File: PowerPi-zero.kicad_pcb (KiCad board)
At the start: 2 copper layers, 65 x 30 mm, 54 parts, among them IC2 TPS51397ARJER, J1 2444, J2 JST XH 01x02, J6 Raspberry_Pi_2_3, J8 JST XH 01x02, Q1 SiA471DJ, Q2 SiA430DJT, U1 LM74700

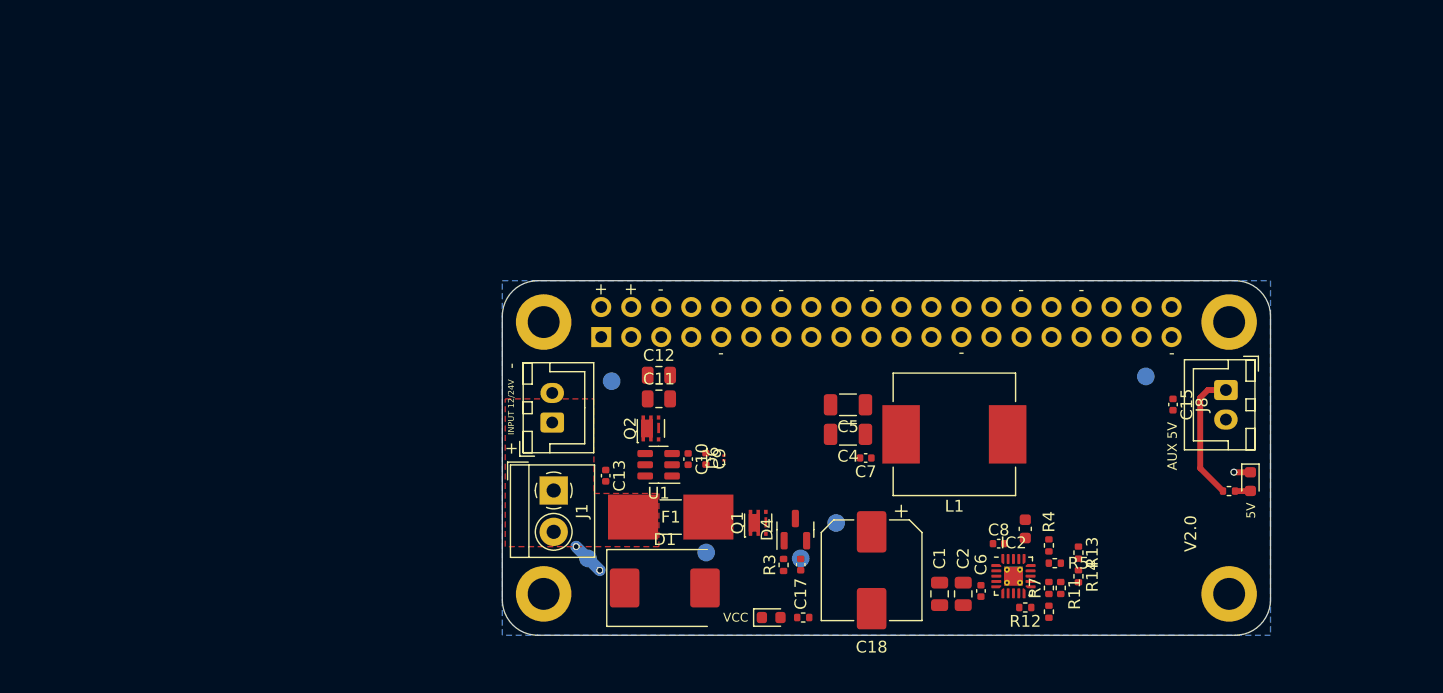
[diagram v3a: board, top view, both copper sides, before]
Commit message: update component position, better layout
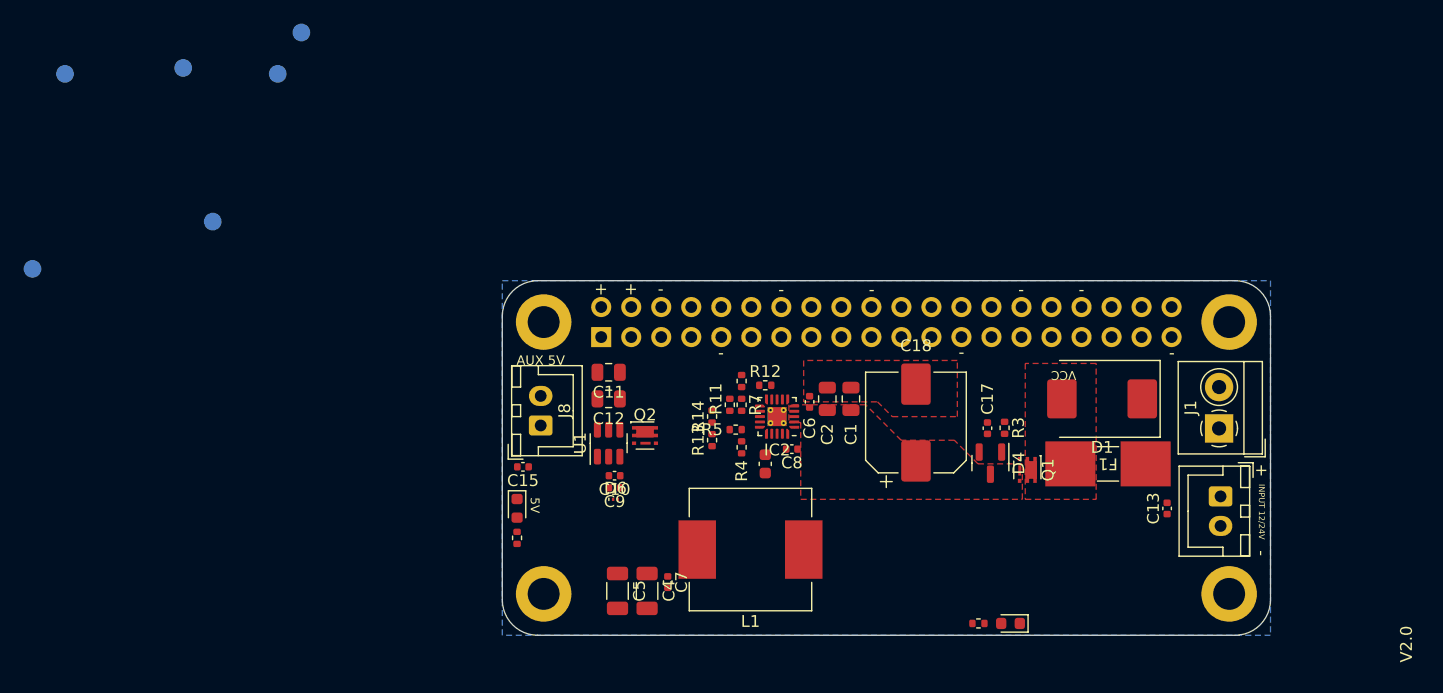
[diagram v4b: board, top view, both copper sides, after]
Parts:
- moved TP1 80.0 mm to (65.2, 88.5)
- moved D3 62.1 mm to (91.0, 112.8)
- moved TP4 61.4 mm to (72.8, 72.5)
- moved R6 60.4 mm to (91.0, 115.3), turned to -90 degrees
- moved TP2 60.3 mm to (52.8, 76.0)
- moved TP3 60.3 mm to (62.8, 75.5)
- moved TP6 60.3 mm to (70.8, 76.0)
- moved J8 58.1 mm to (93.0, 105.8), turned to 90 degrees
- moved J2 56.9 mm to (150.5, 111.8), turned to -90 degrees
- moved J1 56.5 mm to (150.4, 106.0), turned to 90 degrees
- moved C15 55.3 mm to (91.5, 109.2), turned to 180 degrees
- moved TP5 49.9 mm to (50.0, 92.5)
- moved C13 47.6 mm to (146.0, 112.8), turned to 90 degrees
- moved D1 40.3 mm to (140.5, 103.5), turned to 180 degrees
- moved F1 37.3 mm to (141.0, 109.0), turned to 180 degrees
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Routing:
- net +5V: track 11.1 -> 0.00 mm
- net Net-(J1-Pin_1): track 2.83 -> 0.00 mm, vias 2 -> 0
- net GND: track 1.41 -> 0.00 mm, vias 1 -> 0
- net Net-(D3-A): track 1.29 -> 0.00 mm
- added copper zone on F.Cu, net GND
- added copper zone on F.Cu, net Net-(D1-A2)
- added copper zone on F.Cu, net Vin
- removed copper zone on F.Cu, net Net-(J1-Pin_1)

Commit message: layout drafted, silk issues remain
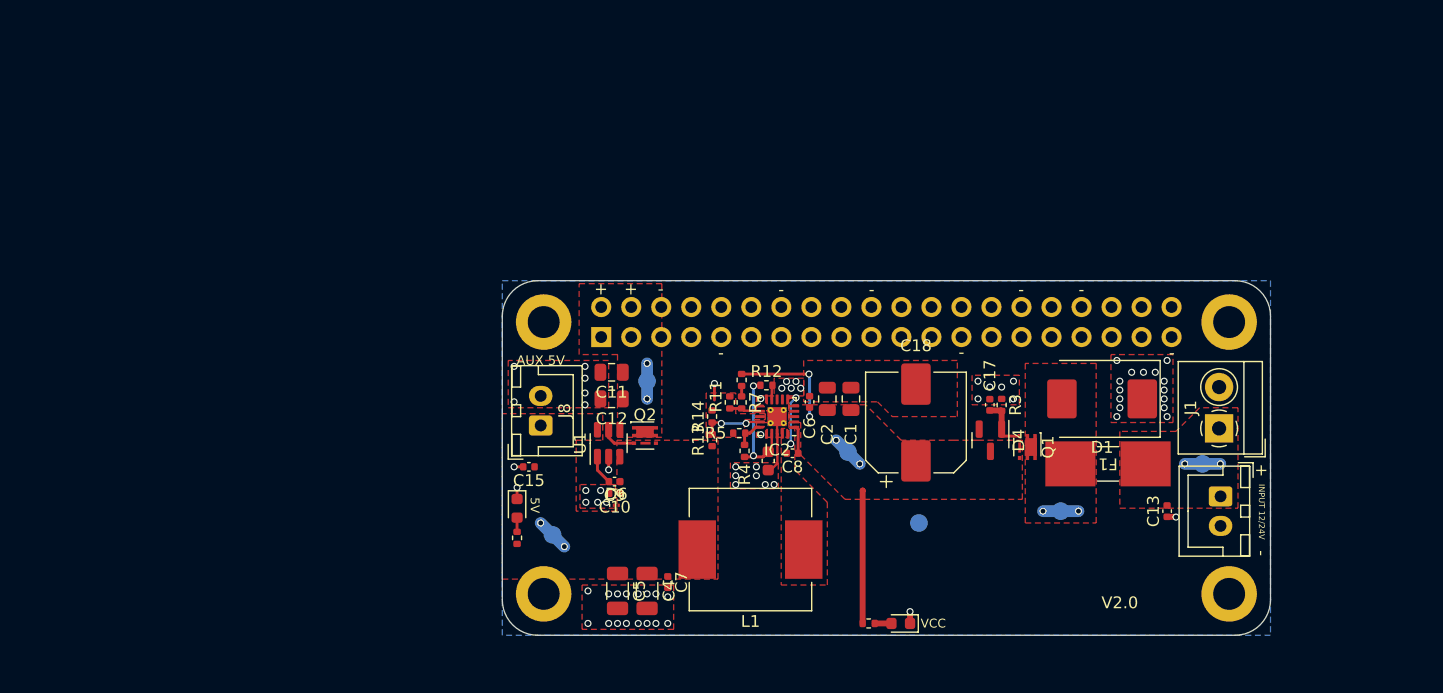
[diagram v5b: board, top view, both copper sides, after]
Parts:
- moved TP2 101.8 mm to (149.0, 109.0)
- moved TP3 83.2 mm to (137.0, 113.0)
- moved TP6 66.2 mm to (125.0, 114.0)
- moved TP4 58.3 mm to (119.0, 108.0)
- moved TP5 52.9 mm to (102.0, 102.0)
- moved TP1 39.1 mm to (94.0, 115.0)
- moved G*** 22.6 mm to (118.0, 117.0)
- moved D5 9.29 mm to (123.5, 122.5)
- moved R8 9.29 mm to (120.8, 122.5)
- moved G*** 9.08 mm to (140.5, 118.0)
- moved C17 1.99 mm to (131.0, 104.0)
- moved R3 1.95 mm to (132.0, 104.0)
- moved D4 1.94 mm to (131.1, 107.0)
- moved Q1 1.94 mm to (134.2, 107.6)
- moved C10 1.50 mm to (99.3, 111.5)
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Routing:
- net Vin: track 0.00 -> 23.4 mm, vias 0 -> 4
- net GND: track 0.00 -> 11.0 mm, vias 0 -> 68
- net VCC: track 0.00 -> 10.4 mm, vias 0 -> 2
- net FB: track 0.00 -> 5.12 mm, vias 0 -> 2
- net SW: track 0.00 -> 4.85 mm, vias 0 -> 2
- net Net-(D4-A): track 0.00 -> 4.67 mm
- net Net-(Q2-G): track 0.00 -> 3.01 mm
- net Net-(J1-Pin_1): track 0.00 -> 3.00 mm, vias 0 -> 2
- net Net-(D1-A2): track 0.00 -> 3.00 mm, vias 0 -> 2
- net 5V_PI: track 0.00 -> 3.00 mm, vias 0 -> 2
- net +5V: track 0.00 -> 2.83 mm, vias 0 -> 2
- net Net-(IC2-EN): track 0.00 -> 2.65 mm
- net Net-(U1-VCAP): track 0.00 -> 2.51 mm
- net Net-(IC2-MODE): track 0.00 -> 2.46 mm
- net BST: track 0.00 -> 2.44 mm
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- added copper zone on F.Cu, net +5V
- added copper zone on F.Cu, net 5V_PI
- added copper zone on F.Cu, net Net-(J1-Pin_1)
- added copper zone on F.Cu, net SW

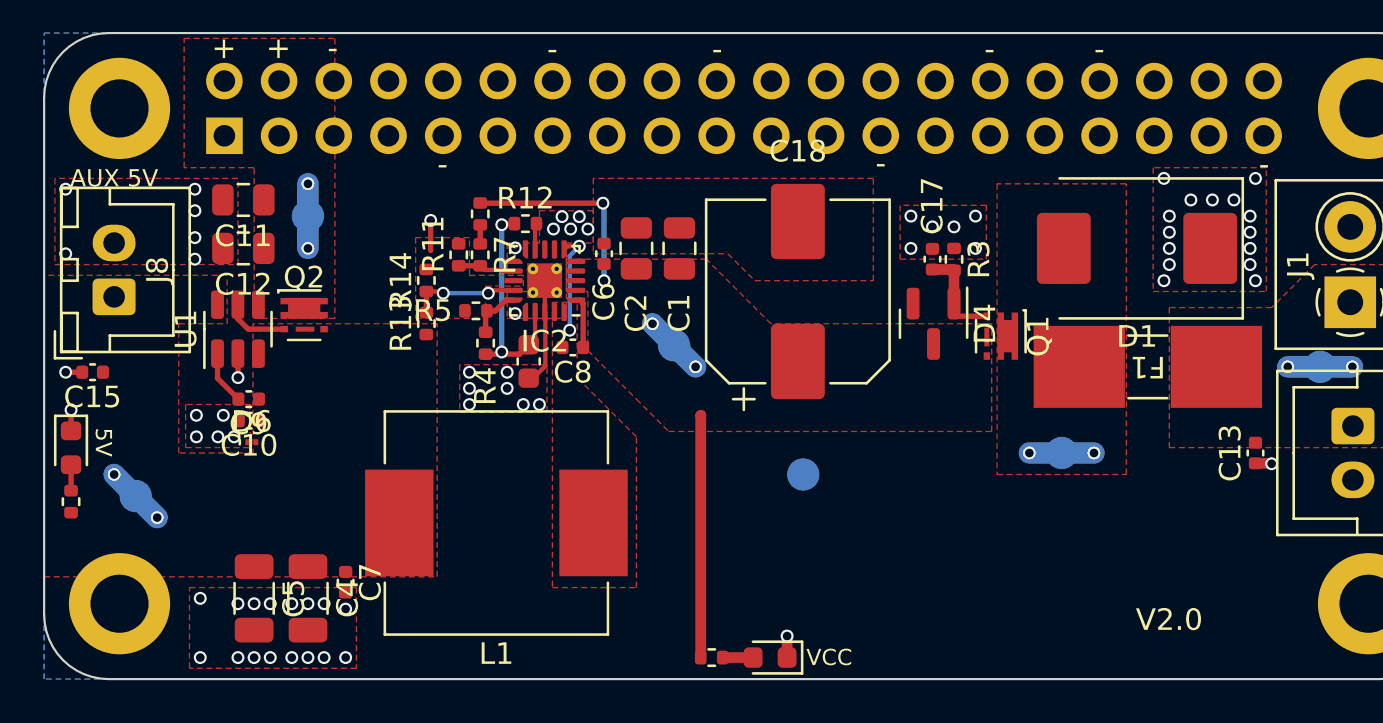
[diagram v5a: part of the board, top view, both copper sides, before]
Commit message: silk fixed, DRC and DFM changes
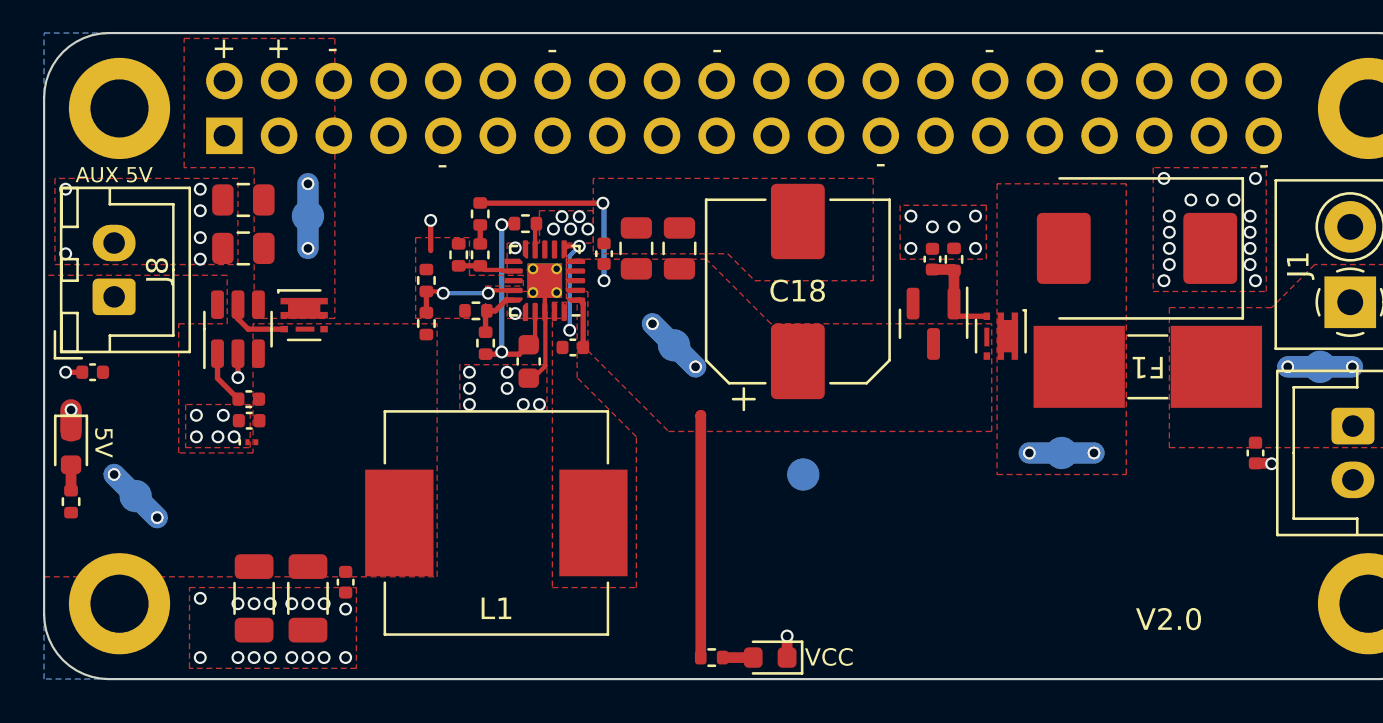
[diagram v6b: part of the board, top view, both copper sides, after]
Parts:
- G***: footprint LOGO -> Graphics:V3D Logo
- G***: footprint Logos:5reen_merge_small -> Graphics:5reen_merge_small
- moved G*** 0.35 mm to (140.2, 117.8)

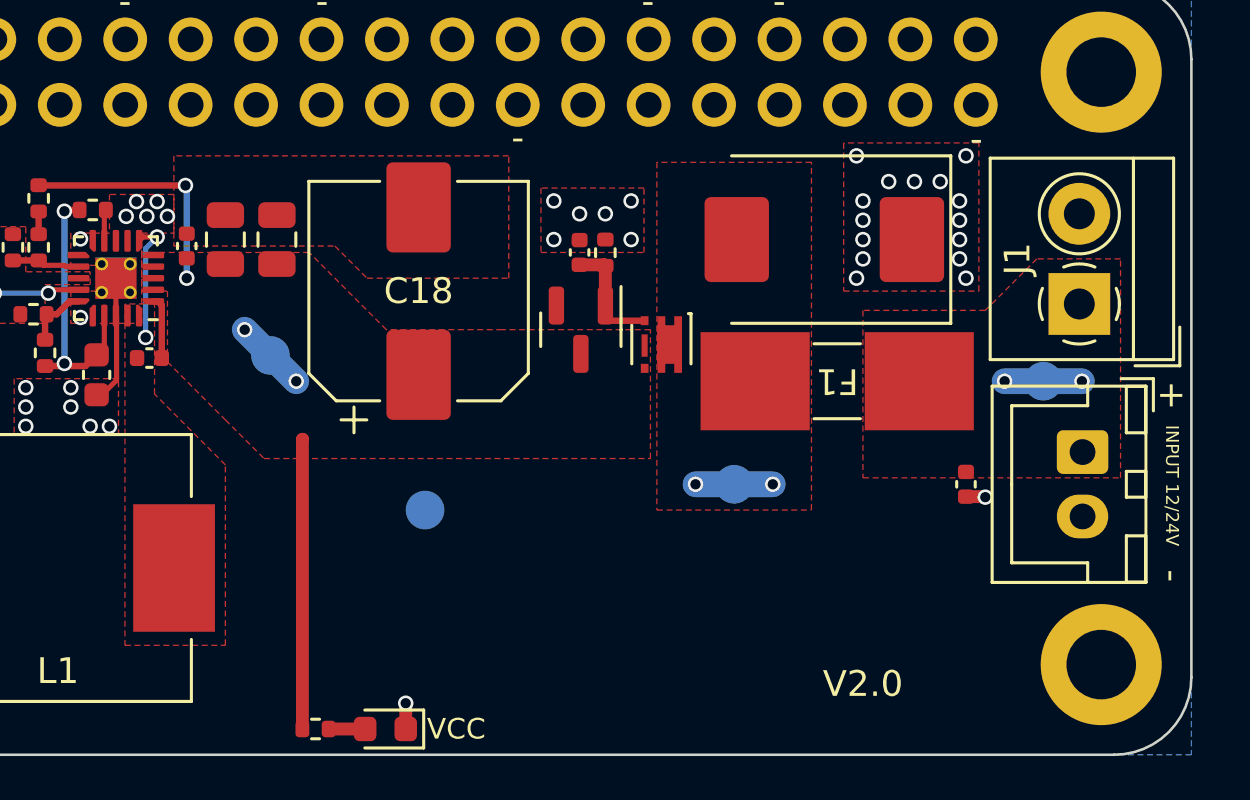
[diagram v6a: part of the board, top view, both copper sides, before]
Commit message: fix thermal connections for pours
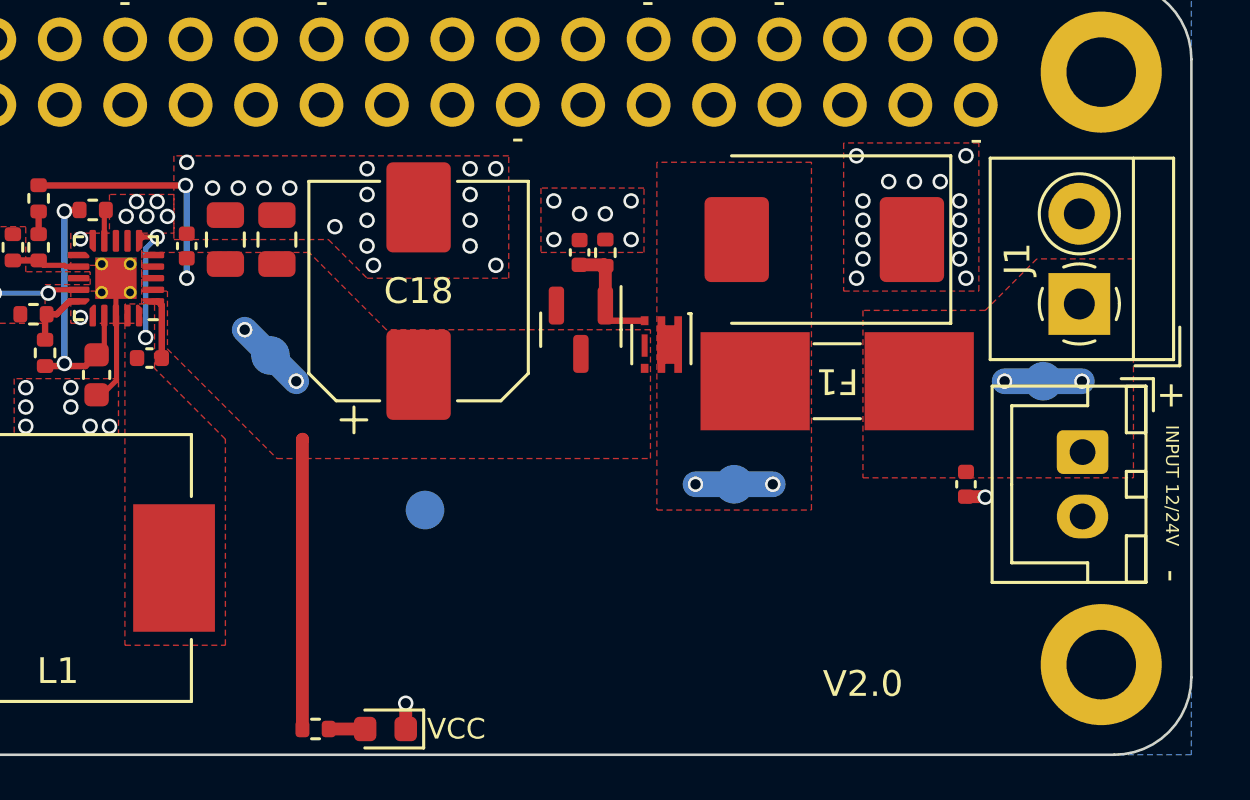
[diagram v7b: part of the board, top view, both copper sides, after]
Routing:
- net GND: vias 68 -> 85
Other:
- board text removed: "Select one of these board edges depending upon the type of socket that is used."
